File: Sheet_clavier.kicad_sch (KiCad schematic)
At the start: 15 parts, among them U6 4021, U7 4021

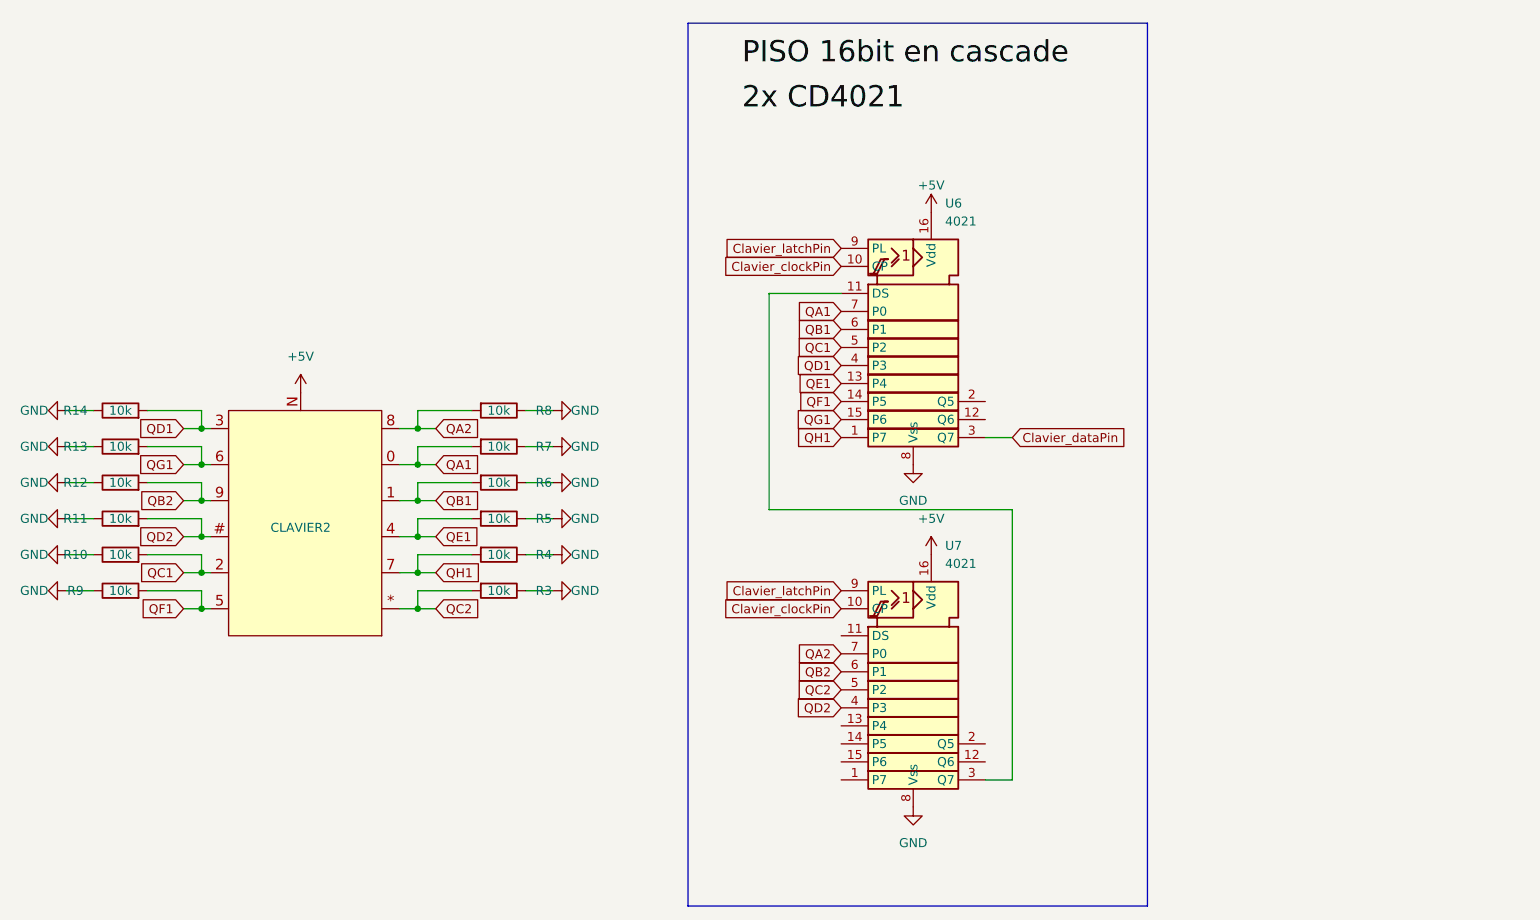
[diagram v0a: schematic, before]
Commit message: changed CD4021 to 74HC299
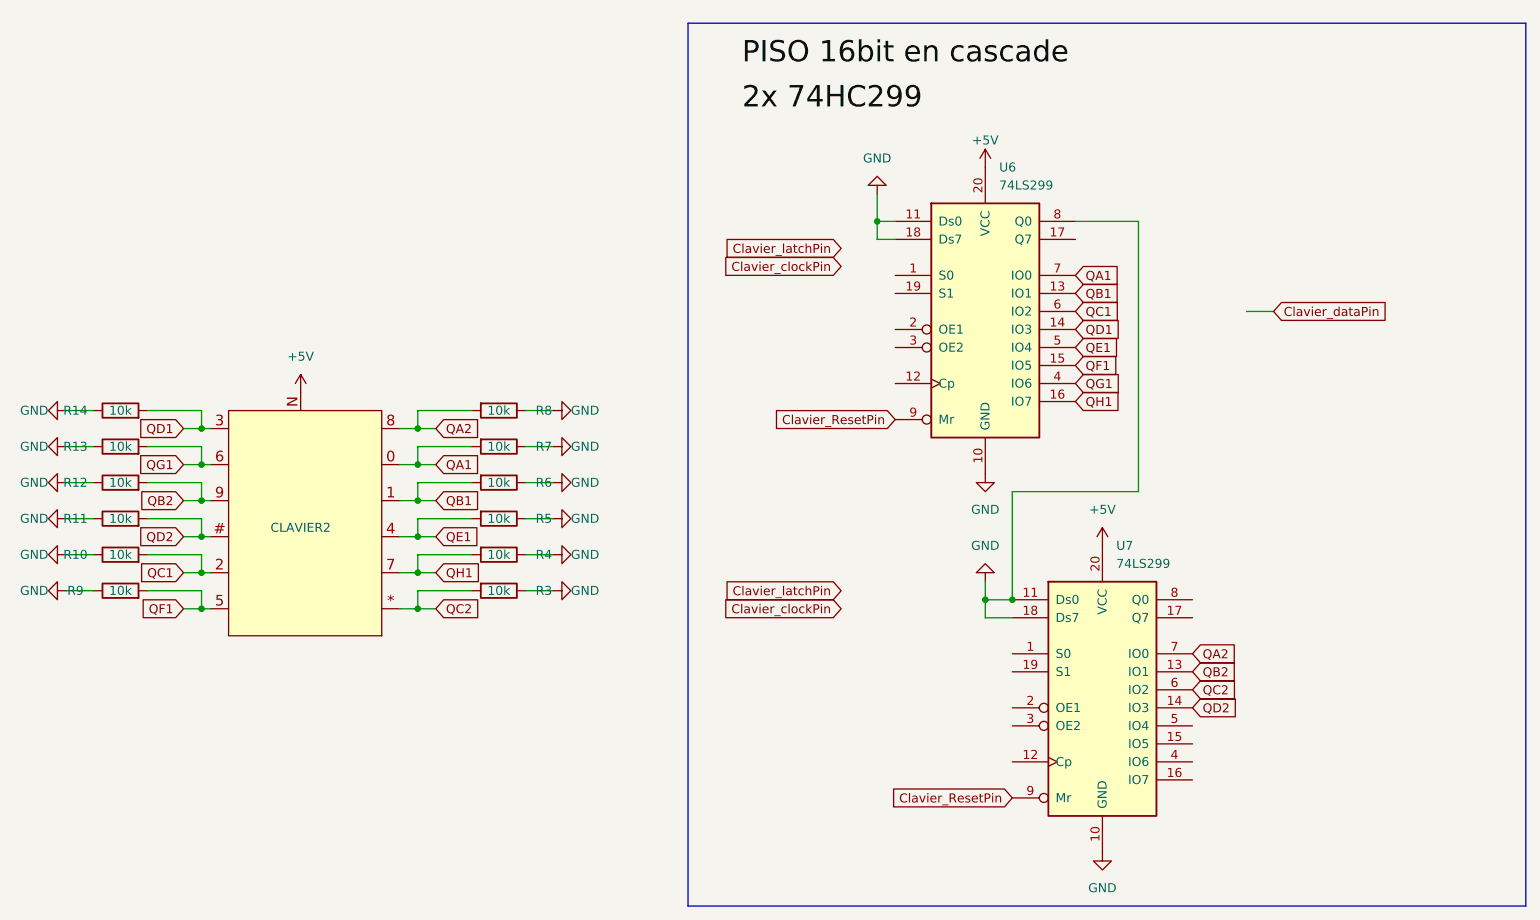
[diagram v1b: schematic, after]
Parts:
- removed U6, U7: 4021, symbol 4xxx_IEEE:4021
- added U6, U7: 74LS299, symbol 74xx:74LS299
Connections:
- net +5V: now also U6.20 (VCC), U7.20 (VCC)
- net GND: now also U6.10 (GND), U6.11 (Ds0), U6.18 (Ds7), U6.8 (Q0), U7.10 (GND), U7.11 (Ds0), U7.18 (Ds7)
- net QA1: now also U6.7 (IO0)
- net QA2: now also U7.7 (IO0)
- net QB1: now also U6.13 (IO1)
- net QB2: now also U7.13 (IO1)
- net QC1: now also U6.6 (IO2)
- net QC2: now also U7.6 (IO2)
- net QD1: now also U6.14 (IO3)
- net QD2: now also U7.14 (IO3)
- net QE1: now also U6.5 (IO4)
- net QF1: now also U6.15 (IO5)
- net QG1: now also U6.4 (IO6)
- net QH1: now also U6.16 (IO7)
- new net Clavier_ResetPin: U6.9 (Mr), U7.9 (Mr)

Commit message: clavier re-update with 4021
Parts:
- removed U6, U7: 74LS299, symbol 74xx:74LS299
- added U6, U7: 4021, symbol 4xxx_IEEE:4021
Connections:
- net +5V: now also U6.16 (Vdd), U7.16 (Vdd)
- net Clavier_clockPin: now also U6.10 (CP), U7.10 (CP)
- net Clavier_dataPin: now also U6.3 (Q7)
- net Clavier_latchPin: now also U6.9 (PL), U7.9 (PL)
- net GND: now also U6.8 (Vss), U7.1 (P7), U7.13 (P4), U7.14 (P5), U7.15 (P6), U7.8 (Vss)
- net QA1: now also U6.7 (P0)
- net QA2: now also U7.7 (P0)
- net QB1: now also U6.6 (P1)
- net QB2: now also U7.6 (P1)
- net QC1: now also U6.5 (P2)
- net QC2: now also U7.5 (P2)
- net QD1: now also U6.4 (P3)
- net QD2: now also U7.4 (P3)
- net QE1: now also U6.13 (P4)
- net QF1: now also U6.14 (P5)
- net QG1: now also U6.15 (P6)
- net QH1: now also U6.1 (P7)
- new net: U6.11 (DS), U7.3 (Q7)
